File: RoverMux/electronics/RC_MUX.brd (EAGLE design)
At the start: 33.5 x 21.6 mm, 24 parts, among them U1 TINY13, U2 MCP1824T, U3 74LS157D

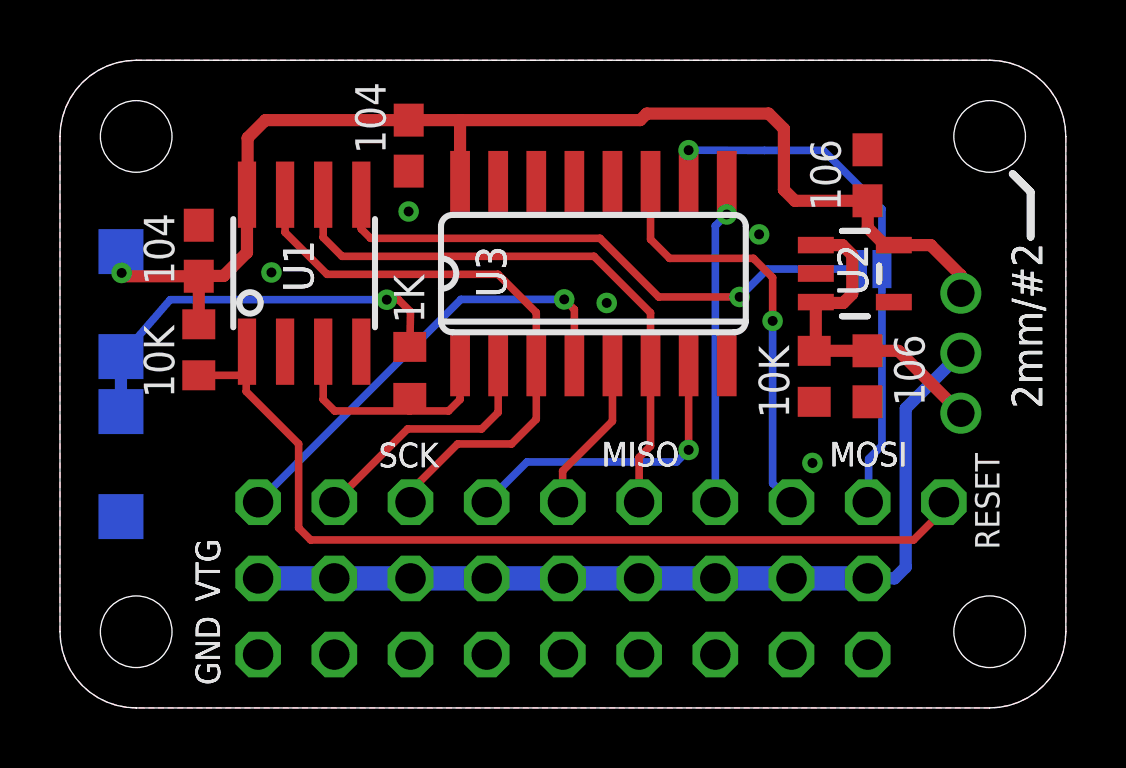
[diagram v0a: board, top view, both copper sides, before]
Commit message: Consolidated RoverMux electronics and software directories under a single top-level directory
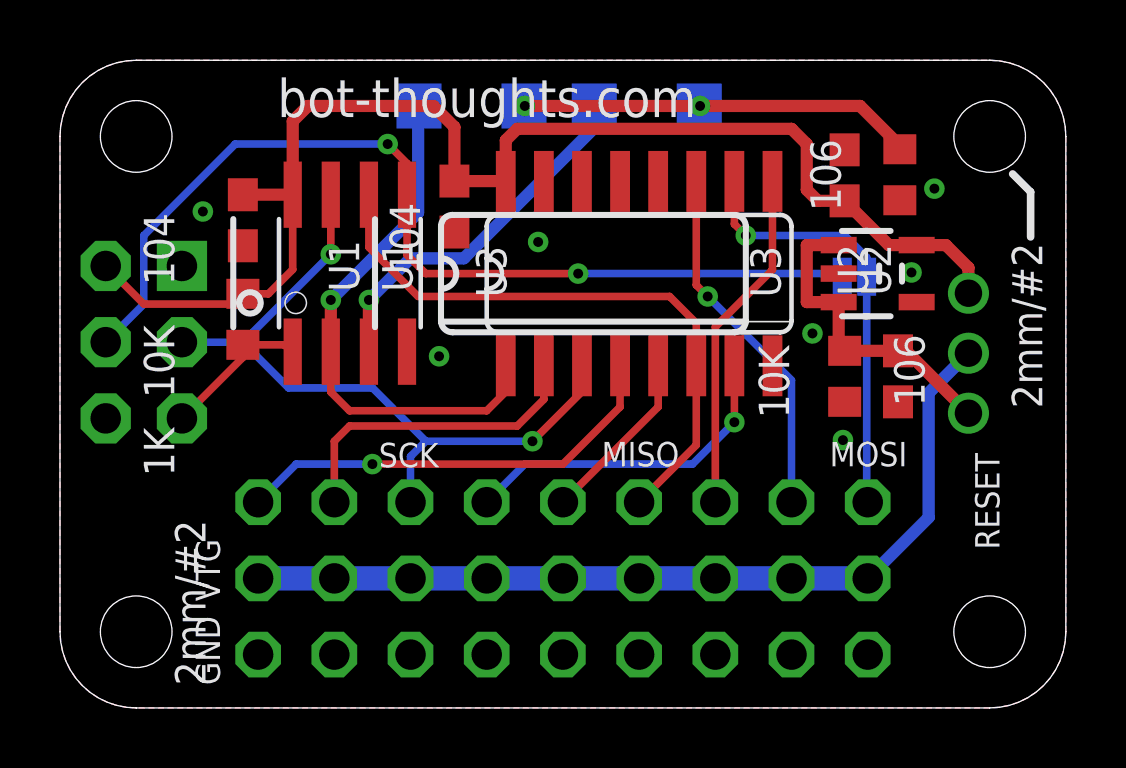
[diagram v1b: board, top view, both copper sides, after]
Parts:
- removed JP2: RESET, pinhead-2:1X01-S
- added J1: ISP, bt_avr:CON6P2R
- moved LED1 18.7 mm to (19.3, 20.1), turned to 90 degrees
- moved R2 17.6 mm to (27.7, 17.8)
- moved LED2 16.7 mm to (13.5, 20.1), turned to 90 degrees
- moved C4 2.54 mm to (12.9, 16.7)
- moved C2 1.79 mm to (5.84, 16.3), turned to 270 degrees
- moved R1 1.79 mm to (5.84, 13.0)
- moved U3 1.52 mm to (19.1, 14.5)
- moved U1 1.52 mm to (9.41, 14.5)
- moved C3 1.02 mm to (27.7, 11.1)
- moved R4 1.02 mm to (25.9, 11.1)
- moved C5 0.76 mm to (25.9, 17.8)
- moved U2 0.76 mm to (27.0, 14.5)
- moved SJ1 0.57 mm to (26.2, 14.4)
- moved JP1 0.25 mm to (30.0, 11.8)
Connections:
- removed net LEDS: LED1.C, LED2.A, R2.1
- removed net N$1: SJ1.1, U1.5
- new net A: LED1.A, U1.3
- new net MISO: J1.1
- new net MOSI: J1.4, SJ1.1, U1.5
- new net N$3: LED1.C, LED2.C, R2.1
- net !RESET: now also J1.5; no longer JP2.1
- net +5V: now also J1.2; no longer LED1.A
- net B: now also LED2.A, U1.2; no longer R2.2, U1.3
- net CH1RX: now also J1.3
- net GND: now also J1.6, R2.2; no longer LED2.C
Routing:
- net MOSI: track 0.00 -> 32.2 mm, vias 0 -> 2
- net !RESET: track 30.5 -> 5.04 mm
- net N$1: track 19.0 -> 0.00 mm, vias 1 -> 0
- net LEDS: track 13.7 -> 0.00 mm, vias 1 -> 0
- net N$3: track 0.00 -> 13.4 mm, vias 0 -> 2
- net A: track 0.00 -> 12.3 mm, vias 0 -> 1
- net B: track 8.03 -> 18.0 mm, vias 0 -> 1
- net CH1RX: track 19.8 -> 24.6 mm, vias 0 -> 2
- net CH3RX: track 18.3 -> 14.5 mm
- net CH1MCU: track 8.25 -> 10.7 mm
- net +5V: track 41.4 -> 43.8 mm, vias 1 -> 0
- net CH3MCU: track 14.3 -> 12.0 mm
- net CH2OUT: track 10.3 -> 11.2 mm
- net REGIN: track 11.8 -> 10.9 mm
- net CH3OUT: track 10.9 -> 11.5 mm, vias 1 -> 0
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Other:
- board text added: "R0.3"
- board text removed: "R0.2"

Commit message: Created RoverMeter for measuring V/A
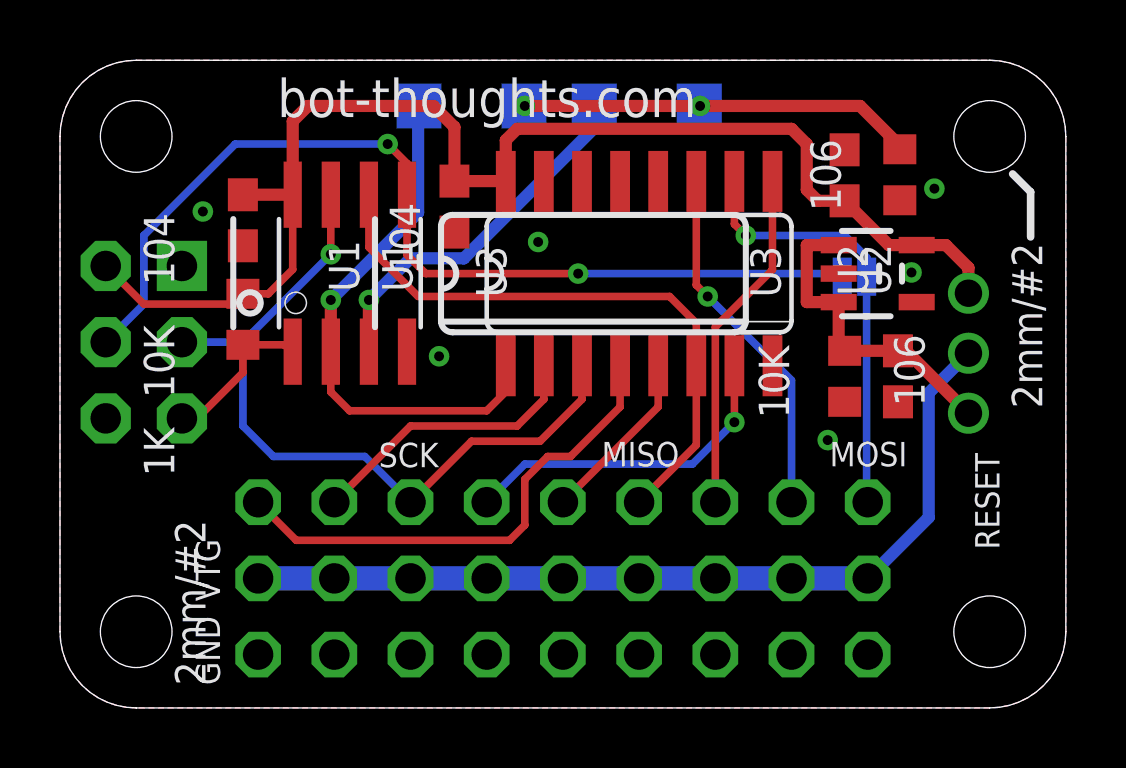
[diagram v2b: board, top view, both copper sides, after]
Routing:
- net CH1OUT: track 14.8 -> 16.7 mm, vias 1 -> 0
- net CH1RX: track 24.6 -> 25.8 mm, vias 2 -> 1
- net CH1MCU: track 10.7 -> 9.52 mm
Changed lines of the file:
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@@
 <contactref element="U3" pad="4"/>
 <wire x1="18.415" y1="11.4046" x2="18.415" y2="10.033" width="0.254" layer="1"/>
-<wire x1="18.415" y1="10.033" x2="16.51" y2="8.128" width="0.254" layer="1"/>
-<wire x1="16.51" y1="8.128" x2="10.16" y2="8.128" width="0.254" layer="1"/>
-<wire x1="10.16" y1="8.128" x2="7.62" y2="8.128" width="0.254" layer="16"/>
-<wire x1="7.62" y1="8.128" x2="6.35" y2="6.858" width="0.254" layer="16"/>
-<via x="10.16" y="8.128" extent="1-16" drill="0.3302"/>
+<wire x1="18.415" y1="10.033" x2="16.764" y2="8.382" width="0.254" layer="1"/>
+<wire x1="16.764" y1="8.382" x2="16.002" y2="8.382" width="0.254" layer="1"/>
+<wire x1="16.002" y1="8.382" x2="15.24" y2="7.62" width="0.254" layer="1"/>
+<wire x1="15.24" y1="7.62" x2="15.24" y2="6.096" width="0.254" layer="1"/>
+<wire x1="15.24" y1="6.096" x2="14.732" y2="5.588" width="0.254" layer="1"/>
+<wire x1="14.732" y1="5.588" x2="7.62" y2="5.588" width="0.254" layer="1"/>
+<wire x1="7.62" y1="5.588" x2="6.35" y2="6.858" width="0.254" layer="1"/>
 </signal>
 <signal name="CH2OUT">
@@
 <wire x1="5.842" y1="12.104" x2="7.2232" y2="12.104" width="0.254" layer="1"/>
 <wire x1="7.2232" y1="12.104" x2="7.503" y2="11.8758" width="0.254" layer="1"/>
-<wire x1="5.842" y1="12.104" x2="5.842" y2="11.684" width="0.254" layer="1"/>
-<wire x1="5.842" y1="11.684" x2="3.81" y2="9.652" width="0.254" layer="1"/>
+<wire x1="5.842" y1="12.104" x2="5.842" y2="11.176" width="0.254" layer="1"/>
+<wire x1="5.842" y1="11.176" x2="4.318" y2="9.652" width="0.254" layer="1"/>
+<wire x1="4.318" y1="9.652" x2="3.81" y2="9.652" width="0.254" layer="1"/>
 </signal>
 <signal name="CH3OUT">
@@
 <contactref element="U2" pad="2"/>
 <contactref element="R4" pad="1"/>
-<via x="24.828" y="12.484" extent="1-16" drill="0.3302"/>
-<polygon width="0.254" layer="1">
+<polygon width="0.254" layer="1" orphans="yes">
 <vertex x="2.286" y="21.59"/>
 <vertex x="30.734" y="21.59" curve="-90"/>
@@
 <via x="28.13" y="14.516" extent="1-16" drill="0.3302"/>
 <via x="28.892" y="17.31" extent="1-16" drill="0.3302"/>
-<via x="25.844" y="8.928" extent="1-16" drill="0.3302"/>
+<via x="25.336" y="8.928" extent="1-16" drill="0.3302"/>
 <via x="4.508" y="16.548" extent="1-16" drill="0.3302"/>
 </signal>
@@
 <wire x1="15.875" y1="11.4046" x2="15.875" y2="10.287" width="0.254" layer="1"/>
 <wire x1="15.875" y1="10.287" x2="14.986" y2="9.398" width="0.254" layer="1"/>
-<wire x1="14.986" y1="9.398" x2="9.398" y2="9.398" width="0.254" layer="1"/>
-<wire x1="9.398" y1="9.398" x2="8.89" y2="8.89" width="0.254" layer="1"/>
-<wire x1="8.89" y1="8.89" x2="8.89" y2="6.858" width="0.254" layer="1"/>
+<wire x1="14.986" y1="9.398" x2="11.43" y2="9.398" width="0.254" layer="1"/>
+<wire x1="11.43" y1="9.398" x2="8.89" y2="6.858" width="0.254" layer="1"/>
 </signal>
 <signal name="CH2MCU">
@@
 <contactref element="U1" pad="7"/>
 <contactref element="J1" pad="3"/>
-<wire x1="17.145" y1="11.4046" x2="17.145" y2="10.541" width="0.254" layer="1"/>
-<wire x1="17.145" y1="10.541" x2="15.494" y2="8.89" width="0.254" layer="1"/>
-<wire x1="15.494" y1="8.89" x2="11.938" y2="8.89" width="0.254" layer="16"/>
-<wire x1="11.938" y1="8.89" x2="11.43" y2="8.382" width="0.254" layer="16"/>
-<wire x1="11.43" y1="8.382" x2="11.43" y2="6.858" width="0.254" layer="16"/>
+<wire x1="17.145" y1="11.4046" x2="17.145" y2="10.287" width="0.254" layer="1"/>
+<wire x1="17.145" y1="10.287" x2="15.748" y2="8.89" width="0.254" layer="1"/>
+<wire x1="15.748" y1="8.89" x2="13.462" y2="8.89" width="0.254" layer="1"/>
+<wire x1="13.462" y1="8.89" x2="11.43" y2="6.858" width="0.254" layer="1"/>
 <wire x1="8.773" y1="17.1082" x2="8.773" y2="15.123" width="0.254" layer="1"/>
+<wire x1="8.773" y1="15.123" x2="5.842" y2="12.192" width="0.254" layer="16"/>
+<wire x1="5.842" y1="12.192" x2="3.81" y2="12.192" width="0.254" layer="16"/>
 <via x="8.773" y="15.123" extent="1-16" drill="0.3302"/>
-<wire x1="5.842" y1="12.192" x2="8.773" y2="15.123" width="0.254" layer="16"/>
-<wire x1="3.81" y1="12.192" x2="5.842" y2="12.192" width="0.254" layer="16"/>
-<via x="15.494" y="8.89" extent="1-16" drill="0.3302"/>
-<wire x1="5.842" y1="12.192" x2="7.366" y2="10.668" width="0.254" layer="16"/>
-<wire x1="7.366" y1="10.668" x2="10.16" y2="10.668" width="0.254" layer="16"/>
-<wire x1="10.16" y1="10.668" x2="11.938" y2="8.89" width="0.254" layer="16"/>
+<wire x1="5.842" y1="12.192" x2="5.842" y2="9.398" width="0.254" layer="16"/>
+<wire x1="5.842" y1="9.398" x2="6.858" y2="8.382" width="0.254" layer="16"/>
+<wire x1="6.858" y1="8.382" x2="9.906" y2="8.382" width="0.254" layer="16"/>
+<wire x1="9.906" y1="8.382" x2="11.43" y2="6.858" width="0.254" layer="16"/>
 </signal>
 <signal name="B">

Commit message: Updated to fix LED indicator circuits, add AVRISP, moved LEDs, rerouted traces.
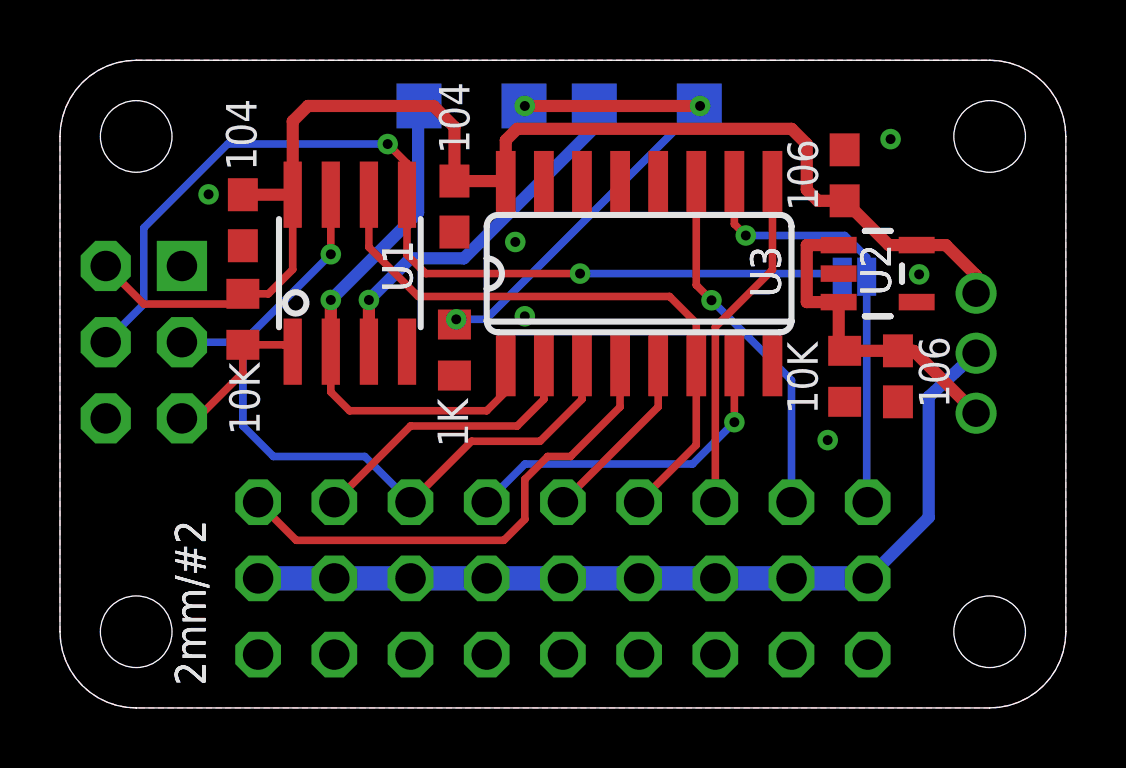
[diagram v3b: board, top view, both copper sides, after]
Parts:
- moved R2 16.0 mm to (12.9, 11.9)
- moved JP1 0.25 mm to (30.3, 11.8)
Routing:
- net N$3: track 13.4 -> 17.3 mm, vias 2 -> 3
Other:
- board text added: "1"
- board text added: "ISP"
- board text removed: "GND"
- board text removed: "MISO"
- board text removed: "MOSI"
- board text removed: "RESET"
- board text removed: "SCK"
- board text removed: "VTG"
